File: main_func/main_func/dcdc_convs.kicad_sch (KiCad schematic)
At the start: 20 parts, among them U6 LMR62421XMF

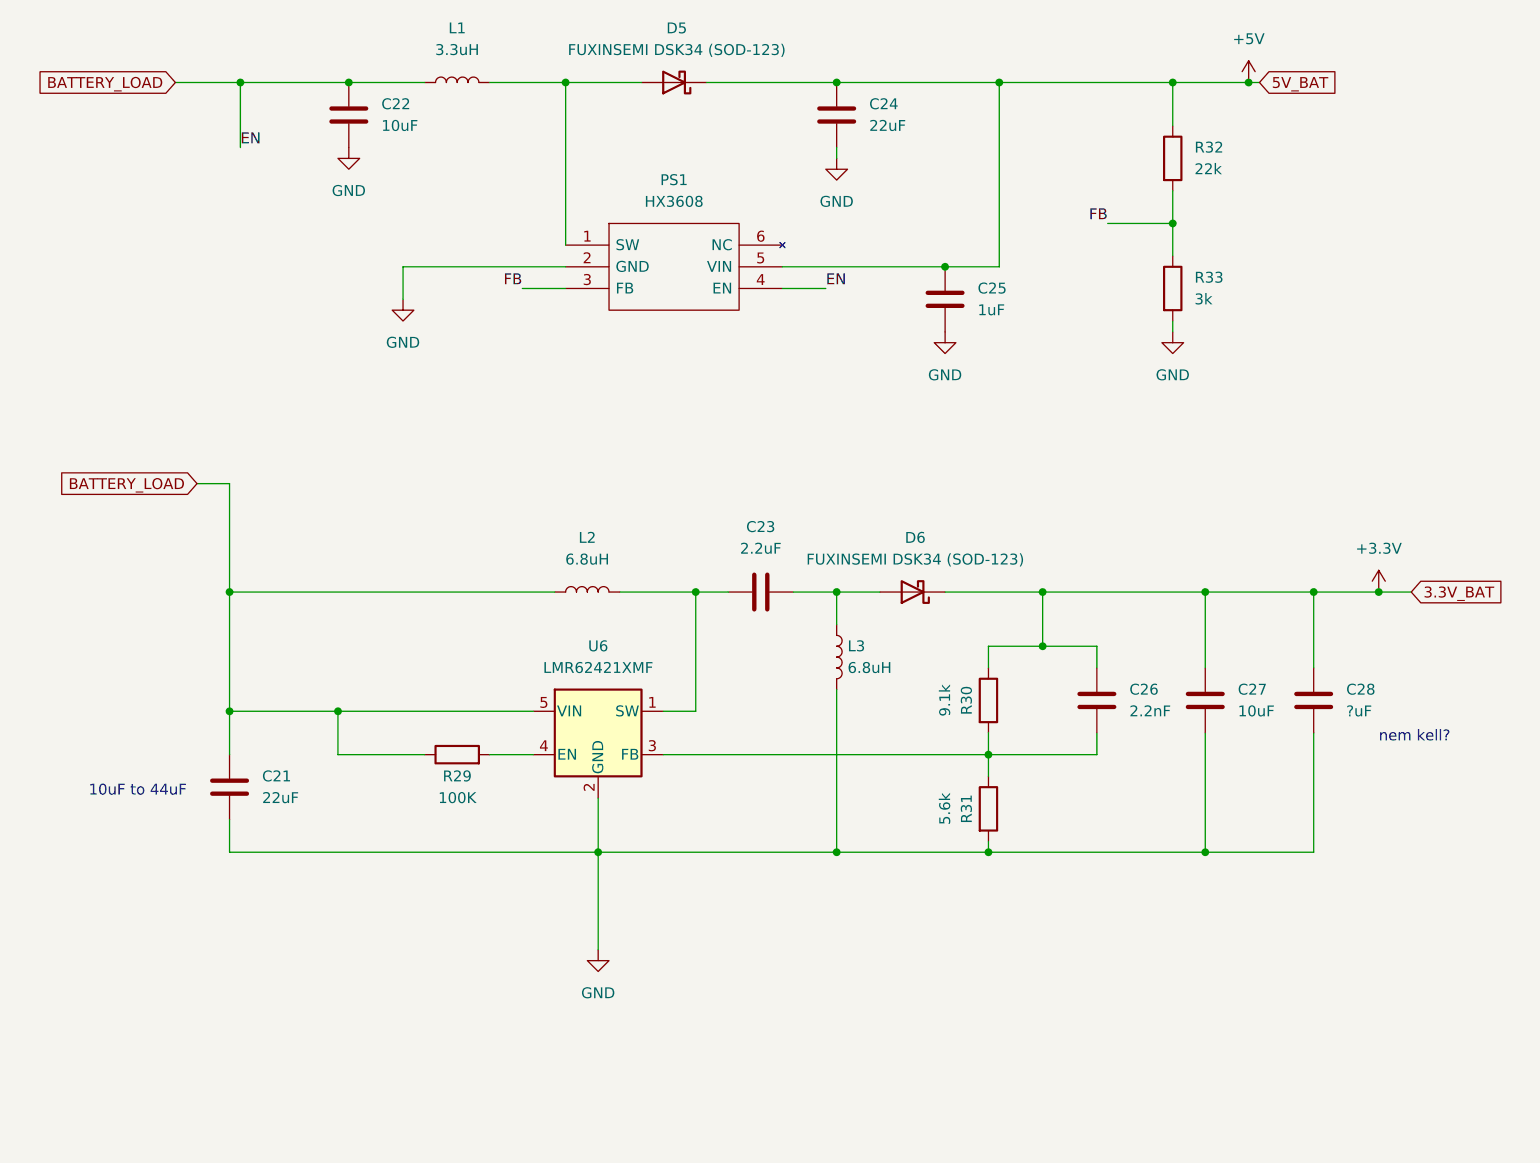
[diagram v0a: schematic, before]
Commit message: main func schematics fixed
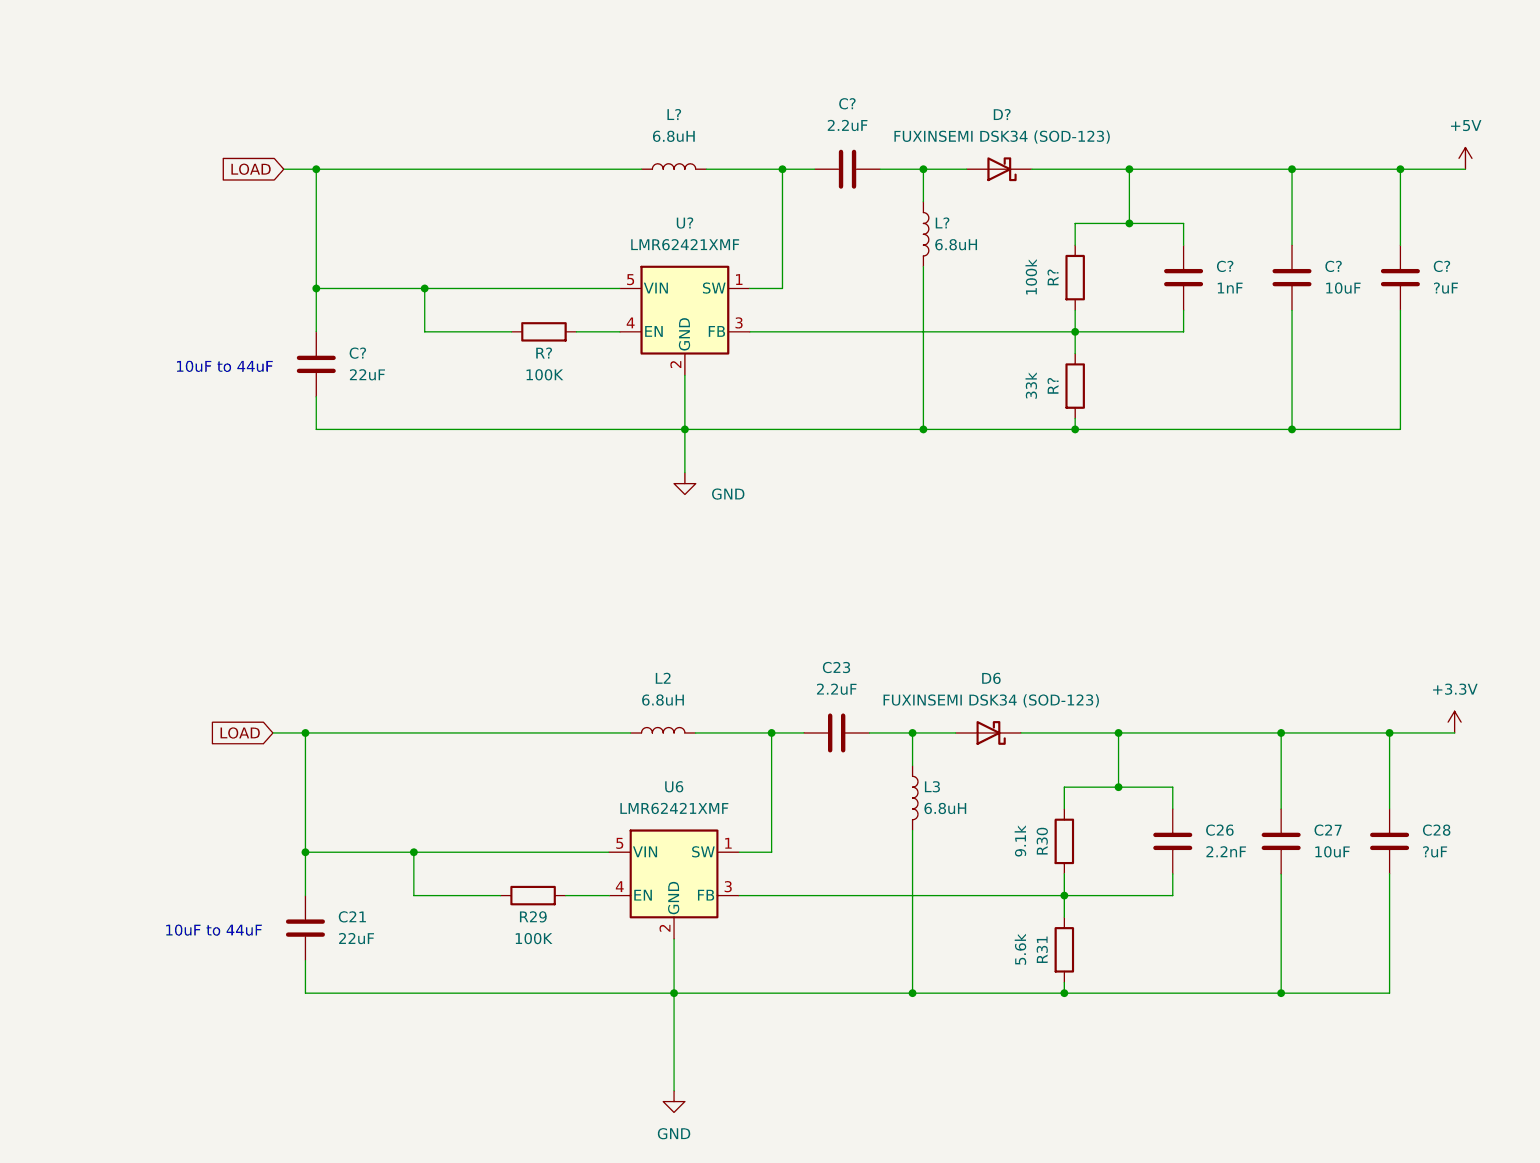
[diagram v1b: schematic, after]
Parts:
- removed C22: 10uF, Capacitor_SMD:C_0805_2012Metric_Pad1.18x1.45mm_HandSolder, symbol Device:C
- removed C24: 22uF, Capacitor_SMD:C_0805_2012Metric_Pad1.18x1.45mm_HandSolder, symbol Device:C
- removed C25: 1uF, Capacitor_SMD:C_0805_2012Metric_Pad1.18x1.45mm_HandSolder, symbol Device:C
- removed D5: FUXINSEMI DSK34 (SOD-123), Diode_SMD:D_SOD-123, symbol Diode:BAT42W-V
- removed L1: 3.3uH, inductors:inductor_koherelec, symbol Device:L
- removed PS1: HX3608, SamacSys_Parts:SOT95P280X125-6N, symbol SamacSys_Parts:HX3608
- removed R32: 22k, Resistor_SMD:R_0805_2012Metric_Pad1.20x1.40mm_HandSolder, symbol Device:R
- removed R33: 3k, Resistor_SMD:R_0805_2012Metric_Pad1.20x1.40mm_HandSolder, symbol Device:R
- added C?: 22uF, Capacitor_SMD:C_0805_2012Metric_Pad1.18x1.45mm_HandSolder, symbol Device:C
- added C?: 2.2uF, Capacitor_SMD:C_0805_2012Metric_Pad1.18x1.45mm_HandSolder, symbol Device:C
- added C?: 1nF, Capacitor_SMD:C_0805_2012Metric_Pad1.18x1.45mm_HandSolder, symbol Device:C
- added C?: ?uF, Capacitor_SMD:C_0805_2012Metric_Pad1.18x1.45mm_HandSolder, symbol Device:C
- added C?: 10uF, Capacitor_SMD:C_0805_2012Metric_Pad1.18x1.45mm_HandSolder, symbol Device:C
- added D?: FUXINSEMI DSK34 (SOD-123), Diode_SMD:D_SOD-123, symbol Diode:BAT42W-V
- added L? (x2): 6.8uH, inductors:inductor_koherelec, symbol Device:L
- added R?: 33k, Resistor_SMD:R_0805_2012Metric_Pad1.20x1.40mm_HandSolder, symbol Device:R
- added R?: 100k, Resistor_SMD:R_0805_2012Metric_Pad1.20x1.40mm_HandSolder, symbol Device:R
- added R?: 100K, Resistor_SMD:R_0805_2012Metric_Pad1.20x1.40mm_HandSolder, symbol Device:R
- added U?: LMR62421XMF, Package_TO_SOT_SMD:SOT-23-5, symbol Regulator_Switching:LMR62421XMF
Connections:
- net +5V: now also C?.1, C?.1, C?.1, D?.1 (K), R?.1
- net GND: now also C?.2, C?.2, C?.2, L?.2, R?.2, U?.2 (GND)
- net BATTERY_LOAD renamed LOAD
- net LOAD: now also C?.1, L?.1, R?.1, U?.5 (VIN)
- new net: C?.2, R?.1, R?.2, U?.3 (FB)
- new net: R?.2, U?.4 (EN)
- new net: C?.1, L?.2, U?.1 (SW)
- new net: C?.2, D?.2 (A), L?.1
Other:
- note removed: "nem kell?"
- moved on the sheet: C21, C23, C26, C27, C28, D6, L2, L3, R29, R30, R31, U6

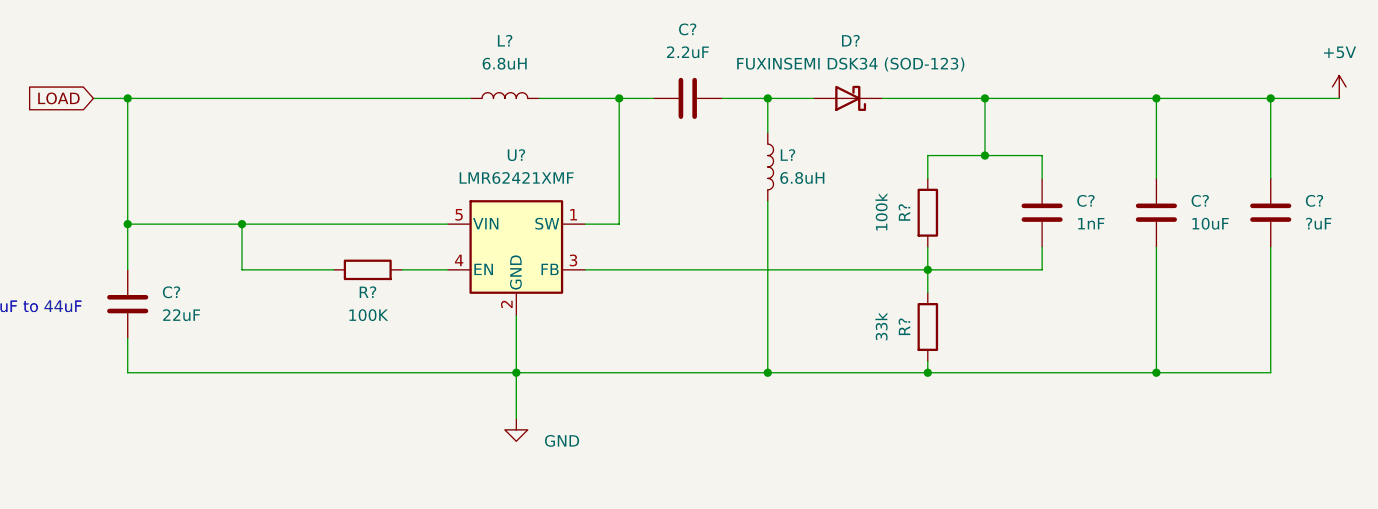
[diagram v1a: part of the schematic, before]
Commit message: fixing keyboard and pot project schematics
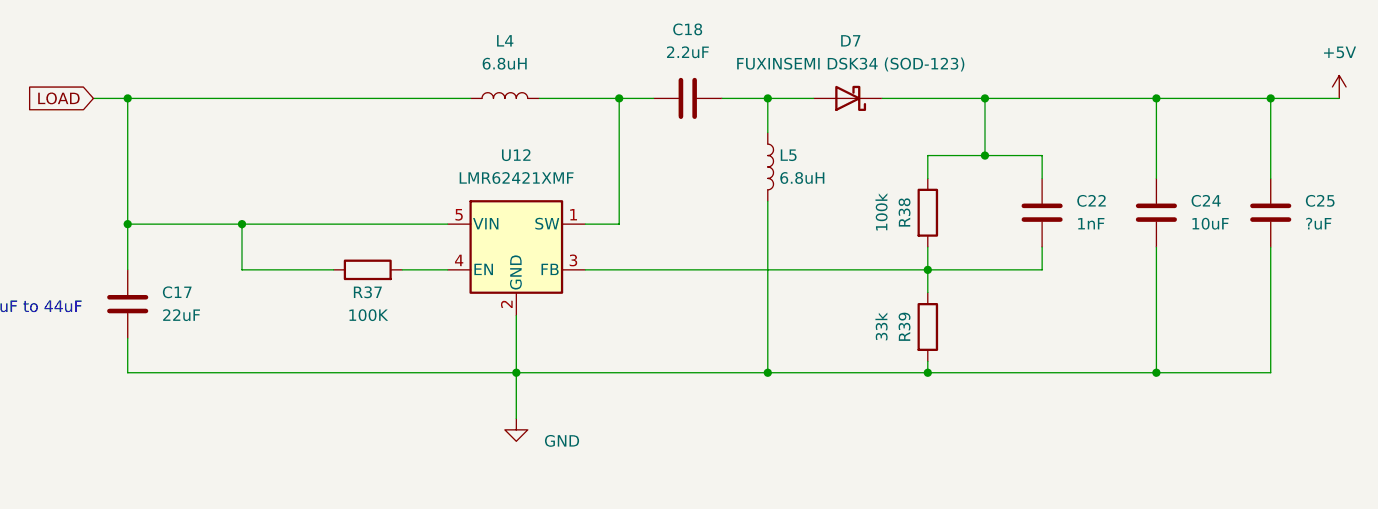
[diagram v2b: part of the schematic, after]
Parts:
- gave numbers to parts that had none: 12
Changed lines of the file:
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@@
   (symbol (lib_id "Device:R") (at 153.67 74.93 0) (unit 1)
     (in_bom yes) (on_board yes)
-    (property "Reference" "R?" (id 0) (at 151.13 74.93 90))
+    (property "Reference" "R39" (id 0) (at 151.13 74.93 90))
     (property "Value" "33k" (id 1) (at 148.59 74.93 90))
     (property "Footprint" "Resistor_SMD:R_0805_2012Metric_Pad1.20x1.40mm_HandSolder" (id 2) (at 151.892 74.93 90)
@@
   (symbol (lib_id "Device:C") (at 64.77 72.39 0) (unit 1)
     (in_bom yes) (on_board yes) (fields_autoplaced)
-    (property "Reference" "C?" (id 0) (at 68.58 71.1199 0)
+    (property "Reference" "C17" (id 0) (at 68.58 71.1199 0)
       (effects (font (size 1.27 1.27)) (justify left))
     )
@@
   (symbol (lib_id "Device:R") (at 153.67 62.23 0) (unit 1)
     (in_bom yes) (on_board yes)
-    (property "Reference" "R?" (id 0) (at 151.13 62.23 90))
+    (property "Reference" "R38" (id 0) (at 151.13 62.23 90))
     (property "Value" "100k" (id 1) (at 148.59 62.23 90))
     (property "Footprint" "Resistor_SMD:R_0805_2012Metric_Pad1.20x1.40mm_HandSolder" (id 2) (at 151.892 62.23 90)
@@
   (symbol (lib_id "power:GND") (at 107.95 85.09 0) (unit 1)
     (in_bom yes) (on_board yes)
-    (property "Reference" "#PWR?" (id 0) (at 107.95 91.44 0)
+    (property "Reference" "#PWR031" (id 0) (at 107.95 91.44 0)
       (effects (font (size 1.27 1.27)) hide)
     )
@@
   (symbol (lib_id "Device:R") (at 91.44 68.58 90) (unit 1)
     (in_bom yes) (on_board yes)
-    (property "Reference" "R?" (id 0) (at 91.44 71.12 90))
+    (property "Reference" "R37" (id 0) (at 91.44 71.12 90))
     (property "Value" "100K" (id 1) (at 91.44 73.66 90))
     (property "Footprint" "Resistor_SMD:R_0805_2012Metric_Pad1.20x1.40mm_HandSolder" (id 2) (at 91.44 70.358 90)
@@
   (symbol (lib_id "Device:C") (at 127 49.53 90) (unit 1)
     (in_bom yes) (on_board yes) (fields_autoplaced)
-    (property "Reference" "C?" (id 0) (at 127 41.91 90))
+    (property "Reference" "C18" (id 0) (at 127 41.91 90))
     (property "Value" "2.2uF" (id 1) (at 127 44.45 90))
     (property "Footprint" "Capacitor_SMD:C_0805_2012Metric_Pad1.18x1.45mm_HandSolder" (id 2) (at 130.81 48.5648 0)
@@
   (symbol (lib_id "power:+5V") (at 199.39 49.53 0) (unit 1)
     (in_bom yes) (on_board yes) (fields_autoplaced)
-    (property "Reference" "#PWR?" (id 0) (at 199.39 53.34 0)
+    (property "Reference" "#PWR032" (id 0) (at 199.39 53.34 0)
       (effects (font (size 1.27 1.27)) hide)
     )
@@
   (symbol (lib_id "Device:L") (at 135.89 57.15 0) (unit 1)
     (in_bom yes) (on_board yes) (fields_autoplaced)
-    (property "Reference" "L?" (id 0) (at 137.16 55.8799 0)
+    (property "Reference" "L5" (id 0) (at 137.16 55.8799 0)
       (effects (font (size 1.27 1.27)) (justify left))
     )
@@
   (symbol (lib_id "Device:C") (at 166.37 62.23 0) (unit 1)
     (in_bom yes) (on_board yes) (fields_autoplaced)
-    (property "Reference" "C?" (id 0) (at 170.18 60.9599 0)
+    (property "Reference" "C22" (id 0) (at 170.18 60.9599 0)
       (effects (font (size 1.27 1.27)) (justify left))
     )
@@
   (symbol (lib_id "Device:L") (at 106.68 49.53 90) (unit 1)
     (in_bom yes) (on_board yes) (fields_autoplaced)
-    (property "Reference" "L?" (id 0) (at 106.68 43.18 90))
+    (property "Reference" "L4" (id 0) (at 106.68 43.18 90))
     (property "Value" "6.8uH" (id 1) (at 106.68 45.72 90))
     (property "Footprint" "inductors:inductor_koherelec" (id 2) (at 106.68 49.53 0)
@@
   (symbol (lib_id "Device:C") (at 191.77 62.23 0) (unit 1)
     (in_bom yes) (on_board yes) (fields_autoplaced)
-    (property "Reference" "C?" (id 0) (at 195.58 60.9599 0)
+    (property "Reference" "C25" (id 0) (at 195.58 60.9599 0)
       (effects (font (size 1.27 1.27)) (justify left))
     )
@@
   (symbol (lib_id "Device:C") (at 179.07 62.23 0) (unit 1)
     (in_bom yes) (on_board yes) (fields_autoplaced)
-    (property "Reference" "C?" (id 0) (at 182.88 60.9599 0)
+    (property "Reference" "C24" (id 0) (at 182.88 60.9599 0)
       (effects (font (size 1.27 1.27)) (justify left))
     )
@@
   (symbol (lib_id "Diode:BAT42W-V") (at 144.78 49.53 180) (unit 1)
     (in_bom yes) (on_board yes) (fields_autoplaced)
-    (property "Reference" "D?" (id 0) (at 145.0975 43.18 0))
+    (property "Reference" "D7" (id 0) (at 145.0975 43.18 0))
     (property "Value" "FUXINSEMI DSK34 (SOD-123)" (id 1) (at 145.0975 45.72 0))
     (property "Footprint" "Diode_SMD:D_SOD-123" (id 2) (at 144.78 45.085 0)
@@
   (symbol (lib_id "Regulator_Switching:LMR62421XMF") (at 107.95 66.04 0) (unit 1)
     (in_bom yes) (on_board yes) (fields_autoplaced)
-    (property "Reference" "U?" (id 0) (at 107.95 55.88 0))
+    (property "Reference" "U12" (id 0) (at 107.95 55.88 0))
     (property "Value" "LMR62421XMF" (id 1) (at 107.95 58.42 0))
     (property "Footprint" "Package_TO_SOT_SMD:SOT-23-5" (id 2) (at 109.22 72.39 0)

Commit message: main_func pcb done
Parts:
- C17, C21: value 22uF -> 22u
- C18, C23: value 2.2uF -> 2.2u
- C22: value 1nF -> 1n
- C24, C27: value 10uF -> 10u
- C25, C28: value ?uF -> ?u
- C26: value 2.2nF -> 2.2n
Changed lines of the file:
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@@
       (effects (font (size 1.27 1.27)) (justify left))
     )
-    (property "Value" "2.2nF" (id 1) (at 168.91 129.5399 0)
+    (property "Value" "2.2n" (id 1) (at 168.91 129.5399 0)
       (effects (font (size 1.27 1.27)) (justify left))
     )
@@
       (effects (font (size 1.27 1.27)) (justify left))
     )
-    (property "Value" "22uF" (id 1) (at 68.58 73.6599 0)
+    (property "Value" "22u" (id 1) (at 68.58 73.6599 0)
       (effects (font (size 1.27 1.27)) (justify left))
     )
@@
     (in_bom yes) (on_board yes) (fields_autoplaced)
     (property "Reference" "C23" (id 0) (at 125.73 107.95 90))
-    (property "Value" "2.2uF" (id 1) (at 125.73 110.49 90))
+    (property "Value" "2.2u" (id 1) (at 125.73 110.49 90))
     (property "Footprint" "Capacitor_SMD:C_0805_2012Metric_Pad1.18x1.45mm_HandSolder" (id 2) (at 129.54 114.6048 0)
       (effects (font (size 1.27 1.27)) hide)
@@
     (in_bom yes) (on_board yes) (fields_autoplaced)
     (property "Reference" "C18" (id 0) (at 127 41.91 90))
-    (property "Value" "2.2uF" (id 1) (at 127 44.45 90))
+    (property "Value" "2.2u" (id 1) (at 127 44.45 90))
     (property "Footprint" "Capacitor_SMD:C_0805_2012Metric_Pad1.18x1.45mm_HandSolder" (id 2) (at 130.81 48.5648 0)
       (effects (font (size 1.27 1.27)) hide)
@@
       (effects (font (size 1.27 1.27)) (justify left))
     )
-    (property "Value" "1nF" (id 1) (at 170.18 63.4999 0)
+    (property "Value" "1n" (id 1) (at 170.18 63.4999 0)
       (effects (font (size 1.27 1.27)) (justify left))
     )
@@
       (effects (font (size 1.27 1.27)) (justify left))
     )
-    (property "Value" "22uF" (id 1) (at 67.31 139.6999 0)
+    (property "Value" "22u" (id 1) (at 67.31 139.6999 0)
       (effects (font (size 1.27 1.27)) (justify left))
     )
@@
       (effects (font (size 1.27 1.27)) (justify left))
     )
-    (property "Value" "?uF" (id 1) (at 194.31 129.5399 0)
+    (property "Value" "?u" (id 1) (at 194.31 129.5399 0)
       (effects (font (size 1.27 1.27)) (justify left))
     )
@@
       (effects (font (size 1.27 1.27)) (justify left))
     )
-    (property "Value" "?uF" (id 1) (at 195.58 63.4999 0)
+    (property "Value" "?u" (id 1) (at 195.58 63.4999 0)
       (effects (font (size 1.27 1.27)) (justify left))
     )
@@
       (effects (font (size 1.27 1.27)) (justify left))
     )
-    (property "Value" "10uF" (id 1) (at 182.88 63.4999 0)
+    (property "Value" "10u" (id 1) (at 182.88 63.4999 0)
       (effects (font (size 1.27 1.27)) (justify left))
     )
@@
       (effects (font (size 1.27 1.27)) (justify left))
     )
-    (property "Value" "10uF" (id 1) (at 181.61 129.5399 0)
-      (effects (font (size 1.27 1.27)) (justify left))
-    )
+    (property "Value" "10u" (id 1) (at 181.61 129.5399 0)
+      (effects (font (size 1.27 1.27)) (justify left))
+    )
